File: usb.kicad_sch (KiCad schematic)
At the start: 37 parts, among them U1 MPFS250T-FCVG484, U12 SN74LVC1G04_SOT, U13 USB3340-EZK-TR, Y1 Resonator_24MHz_CTS_SA324

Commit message: [#54828] Add USB hub, change LBEE5PK2AE connection to USB
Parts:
- added U20: USB3803, antmicro-footprints:WLCSP-25_2.05x2.05mm_Layout5x5_P0.4x0.4mm_NSMD, symbol antmicroInterfaceControllers:USB3803
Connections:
- net USB_N: now also U20.E1 (USBUP_DM)
- net USB_P: now also U20.E2 (USBUP_DP)
- new net CONN_USB_N: U20.D1 (USBDN3_DM)
- new net CONN_USB_P: U20.C1 (USBDN3_DP)
- new net WL_BT_USB_DM: U20.D2 (USBDN2_DM)
- new net WL_BT_USB_DP: U20.C2 (USBDN2_DP)
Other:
- note added: "USB HUB"
- moved on the sheet: C118, C119, C120, C121, C122, C123, C124, D3, D4, D5, FB1, R58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

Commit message: [#54828] Add connections and external components to USB hub
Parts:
- added C258: C_1u_0402, antmicro-footprints:C_0402_1005Metric, symbol antmicroCapacitors0402:C_1u_0402
- added C259: C_4u7_0402, antmicro-footprints:C_0402_1005Metric, symbol antmicroCapacitors0402:C_4u7_0402
- added C260, C261, C262: C_100n_0402, antmicro-footprints:C_0402_1005Metric, symbol antmicroCapacitors0402:C_100n_0402
- added R100, R101, R102, R112, R113, R114, R115, R116, R117, R118, R119, R120, R98: R_10k_0402, antmicro-footprints:R_0402_1005Metric, symbol antmicroResistors0402:R_10k_0402
- added R99: R_12k_0402, antmicro-footprints:R_0402_1005Metric, symbol antmicroResistors0402:R_12k_0402
- added Y4: Oscillator_26MHz_ESC_2520MV, antmicro-footprints:Oscillator_SMD_ECS_2520MV_2.5x2mm, symbol antmicroOscillators:Oscillator_26MHz_ESC_2520MV
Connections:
- net +3V3: now also U20.B2 (VBAT), C260.2, C262.2, R100.2, R102.2, R113.2, R115.2, R98.2, Y4.1 (EN), Y4.4 (VDD)
- net CONN_USB_N: now also D4.2
- net CONN_USB_P: now also D5.2
- net GND: now also U20.C3 (GND), C258.1, C259.1, C260.1, C261.1, C262.1, R101.1, R112.1, R114.1, R116.1, R99.1, Y4.2 (GND)
- net USB_N: no longer D4.2
- net USB_OTG_ID: now also U20.A5 (BYPASS_N), R98.1
- net USB_P: no longer D5.2
- net SPK_L: now reaches R61.1, R62.2, TP2.1, U13.15 (SPK_L)
- net SPK_R: now reaches R59.1, R60.2, TP1.1, U13.16 (SPK_R)
- net VDD33_BYP: now reaches U20.A1 (USBDN1_DP)
- net VDD33_BYP: now also U20.A2 (VDD33_BYP), U20.B1 (USBDN1_DM), U20.B5 (HUB_CONNECT), C259.2
- net +1V8: now reaches U20.A3 (VDD_CORE_REG)
- net +1V8: now also C261.2
- net RBIAS: now reaches U20.A4 (RBIAS)
- net RBIAS: now also R99.2
- net REF_CLK: now reaches U20.B3 (REFCLK)
- net REF_CLK: now also Y4.3 (OUT)
- net I2C_ASEL1: now reaches U20.B4 (I2C_ASEL1)
- net I2C_ASEL1: now also R100.1, R101.2
- net I2C_ASEL0: now reaches U20.C4 (I2C_ASEL0)
- net I2C_ASEL0: now also R102.1, R112.2
- net USB_HUB_INT_N: now reaches U20.C5 (INT_N)
- net USB_HUB_INT_N: now also U1.D3 (MSSIO28B2), R119.1
- net VDD12_BYP: now reaches U20.D3 (VDD12_BYP)
- net VDD12_BYP: now also C258.2
- net REF_SEL1: now reaches U20.D4 (REF_SEL1)
- net REF_SEL1: now also R113.1, R114.2
- net USB_HUB_SDA: now reaches U20.D5 (SDA)
- net USB_HUB_SDA: now also U1.B1 (MSSIO27B2), R118.1
- net USB_HUB_RESET: now reaches U20.E3 (RESET_N)
- net USB_HUB_RESET: now also U1.C2 (MSSIO29B2), R120.1
- net REF_SEL0: now reaches U20.E4 (REF_SEL0)
- net REF_SEL0: now also R115.1, R116.2
- net USB_HUB_SCL: now reaches U20.E5 (SCL)
- net USB_HUB_SCL: now also U1.C1 (MSSIO26B2), R117.1
- new net VDDI: R117.2, R118.2, R119.2, R120.2
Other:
- note added: "HUB CLK"
- note added: "HUB FREQ CONFIG"
- note added: "HUB I2C ADDR CONFIG"
- note added: "I2C_ASEL[1:0]| I2C address '00' | 0x10 '01' | 0x11 '10' | 0x50 '11' | 0x51"
- note added: "REF_SEL[1:0] | Frequency (MHz) '00' | 38.4 '01' | 26.0 '10' | 19.2 '11' | 12.0"
- moved on the sheet: R64, TP1, TP2, TP3, TP4, U20

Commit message: [#54016] Change 100nF to 0201 package
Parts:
- C118, C119, C120, C121, C122, C123, C124: value C_100n_25V_0402 -> C_100n_0201_25V; footprint antmicro-footprints:C_0402_1005Metric -> antmicro-footprints:C_0201; symbol antmicroCapacitors0402:C_100n_25V_0402 -> antmicroCapacitorsmisc:C_100n_0201_25V; MPN CL05A104KA5NNNC -> C0603X5R1E104K030BB; Manufacturer Murata -> TDK
- C260, C261, C262: value C_100n_0402 -> C_100n_0201_25V; footprint antmicro-footprints:C_0402_1005Metric -> antmicro-footprints:C_0201; symbol antmicroCapacitors0402:C_100n_0402 -> antmicroCapacitorsmisc:C_100n_0201_25V; MPN GRM155R61H104KE14D -> C0603X5R1E104K030BB; Manufacturer Murata -> TDK; Voltage 50V -> 25V

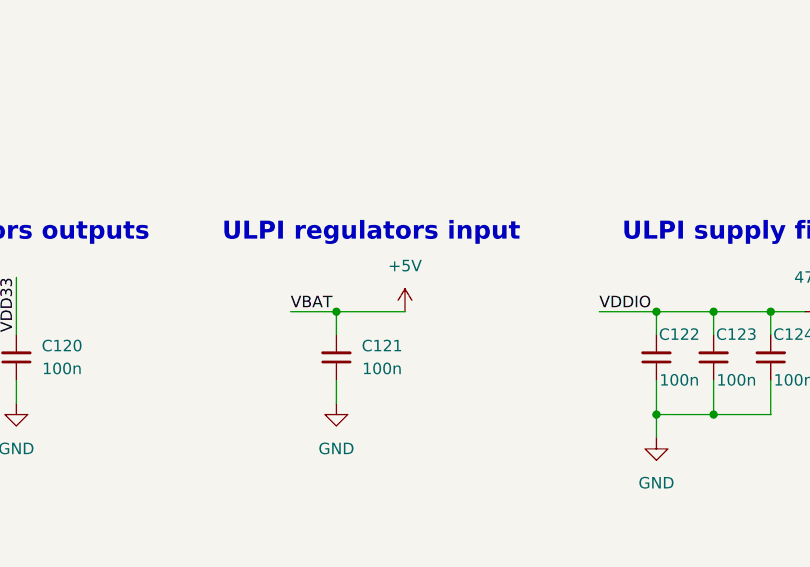
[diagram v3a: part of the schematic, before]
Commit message: [#54491] Change VBAT in USB Phy to 3V3
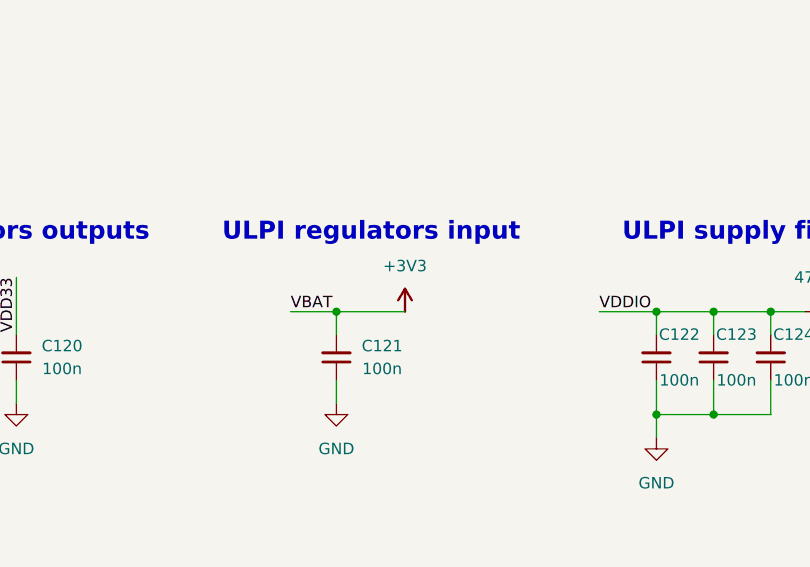
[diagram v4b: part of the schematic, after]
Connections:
- net +5V is gone; now on net +3V3: C121.2, U13.21 (VBAT)
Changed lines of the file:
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@@
     )
   )
+  (symbol (lib_id "antmicropower:+3V3") (at 85.09 57.15 0) (unit 1)
+    (in_bom yes) (on_board yes) (dnp no) (fields_autoplaced)
+    (property "Reference" "#PWR020" (at 100.33 59.69 0)
+      (effects (font (size 1.27 1.27) (thickness 0.15)) (justify left bottom) hide)
+    )
+    (property "Value" "+3V3" (at 85.09 52.07 0)
+      (effects (font (size 1.27 1.27) (thickness 0.15)))
+    )
+    (property "Footprint" "" (at 100.33 64.77 0)
+      (effects (font (size 1.27 1.27) (thickness 0.15)) (justify left bottom) hide)
+    )
+    (property "Datasheet" "" (at 100.33 67.31 0)
+      (effects (font (size 1.27 1.27) (thickness 0.15)) (justify left bottom) hide)
+    )
+    (property "Author" "Antmicro" (at 100.33 64.77 0)
+      (effects (font (size 1.27 1.27) (thickness 0.15)) (justify left bottom) hide)
+    )
+    (property "License" "Apache-2.0" (at 100.33 67.31 0)
+      (effects (font (size 1.27 1.27) (thickness 0.15)) (justify left bottom) hide)
+    )
+    (pin "1")
+    (instances
+      (project "polarfire-som"
+        (path "/db4a0d3e-2eb3-499e-977d-6eb378cfd3ed/d93d65d4-e21e-44e3-82fb-4ad52468a6b3"
+          (reference "#PWR020") (unit 1)
+        )
+      )
+    )
+  )
   (symbol (lib_id "antmicroResistors0402:R_10k_0402") (at 80.01 236.22 270) (mirror x) (unit 1)
     (in_bom yes) (on_board yes) (dnp no)
@@
         )
       )
-    )
-  )
-  (symbol (lib_id "antmicropower:+5V") (at 85.09 57.15 0) (unit 1)
-    (in_bom yes) (on_board yes) (dnp no) (fields_autoplaced)
-    (property "Reference" "#PWR0312" (at 100.33 59.69 0)
-      (effects (font (size 1.27 1.27) (thickness 0.15)) (justify left bottom) hide)
-    )
-    (property "Value" "+5V" (at 85.09 52.07 0)
-      (effects (font (size 1.27 1.27) (thickness 0.15)))
-    )
-    (property "Footprint" "" (at 100.33 64.77 0)
-      (effects (font (size 1.27 1.27) (thickness 0.15)) (justify left bottom) hide)
-    )
-    (property "Datasheet" "" (at 100.33 67.31 0)
-      (effects (font (size 1.27 1.27) (thickness 0.15)) (justify left bottom) hide)
-    )
-    (property "Author" "Antmicro" (at 100.33 64.77 0)
-      (effects (font (size 1.27 1.27) (thickness 0.15)) (justify left bottom) hide)
-    )
-    (property "License" "Apache-2.0" (at 100.33 67.31 0)
-      (effects (font (size 1.27 1.27) (thickness 0.15)) (justify left bottom) hide)
-    )
-    (pin "1")
-    (instances
-      (project "polarfire-som"
-        (path "/db4a0d3e-2eb3-499e-977d-6eb378cfd3ed/d93d65d4-e21e-44e3-82fb-4ad52468a6b3"
-          (reference "#PWR0312") (unit 1)
-        )
-      )

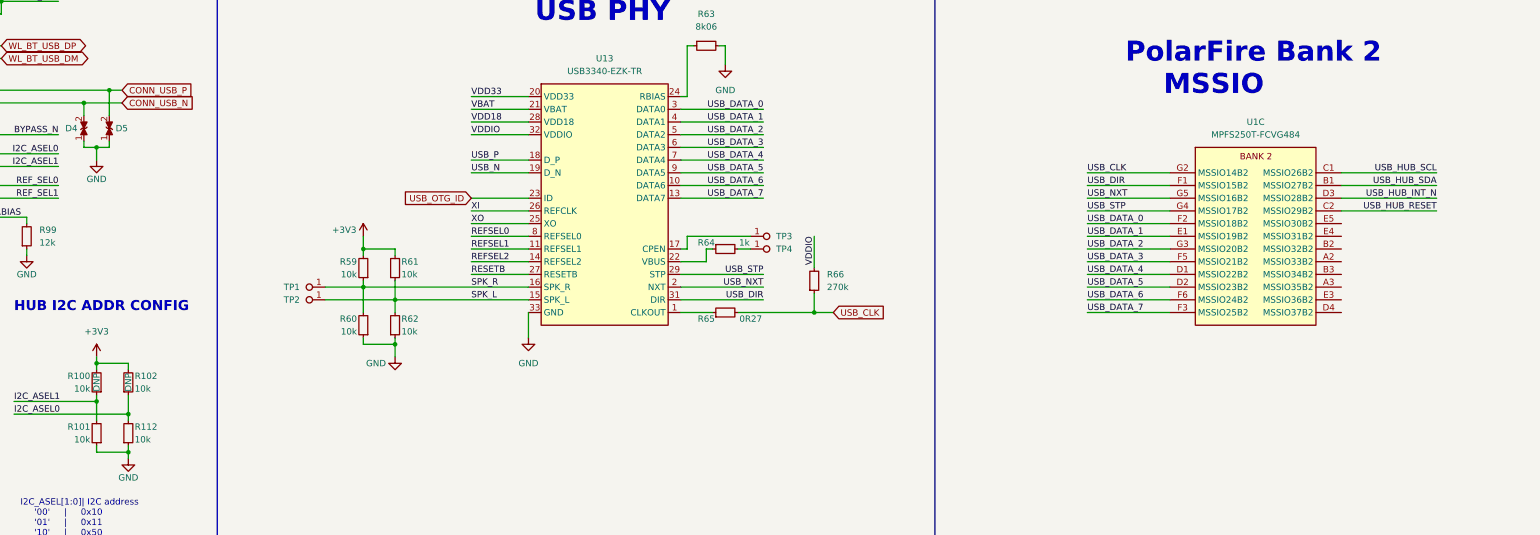
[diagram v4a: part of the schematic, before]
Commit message: [#54016] Add PAC1934 to MSSIO I2C_1, change USB hub default address
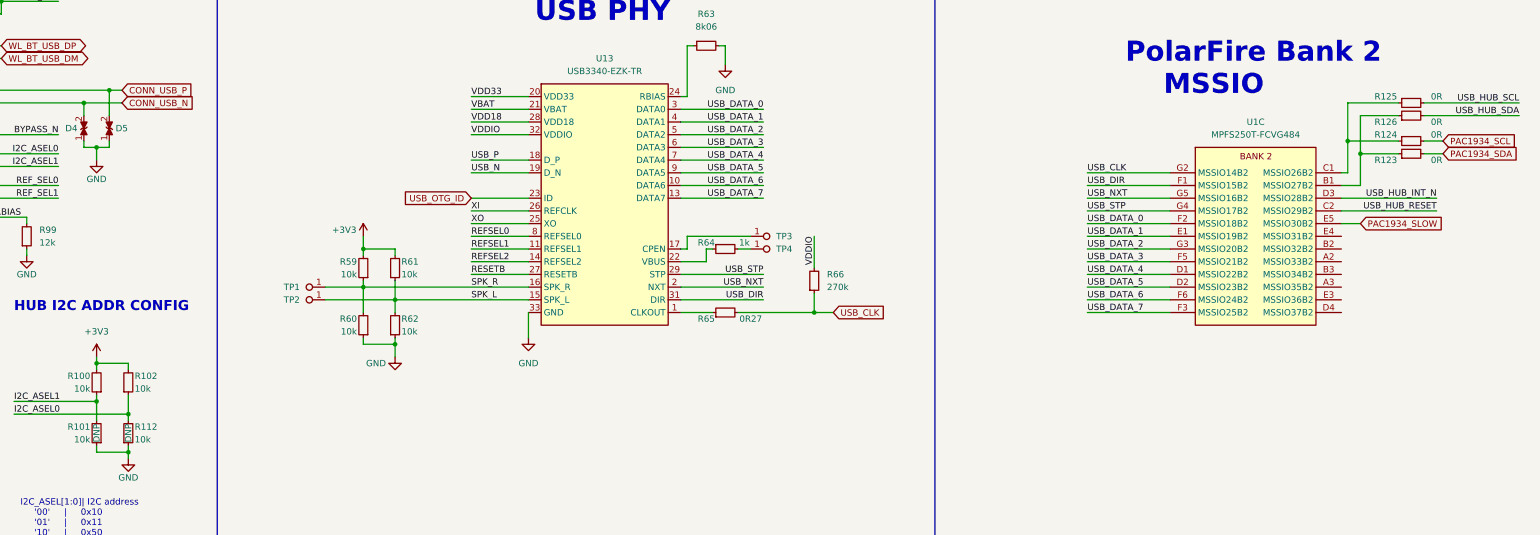
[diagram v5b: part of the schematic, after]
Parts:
- added R123, R124, R125, R126: R_0R_0402, antmicro-footprints:R_0402_1005Metric, symbol antmicroResistors0402:R_0R_0402
- R100, R102: DNP DNP -> (none); now in the parts list
- R101, R112: DNP (none) -> DNP; now left out of the parts list
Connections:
- net USB_HUB_SCL: now also R125.2; no longer U1.C1 (MSSIO26B2)
- net USB_HUB_SDA: now also R126.2; no longer U1.B1 (MSSIO27B2)
- net PAC1934_SLOW: now reaches U1.E5 (MSSIO30B2)
- new net: R123.1, R126.1, U1.B1 (MSSIO27B2)
- new net: R124.1, R125.1, U1.C1 (MSSIO26B2)
- new net PAC1934_SCL: R124.2
- new net PAC1934_SDA: R123.2

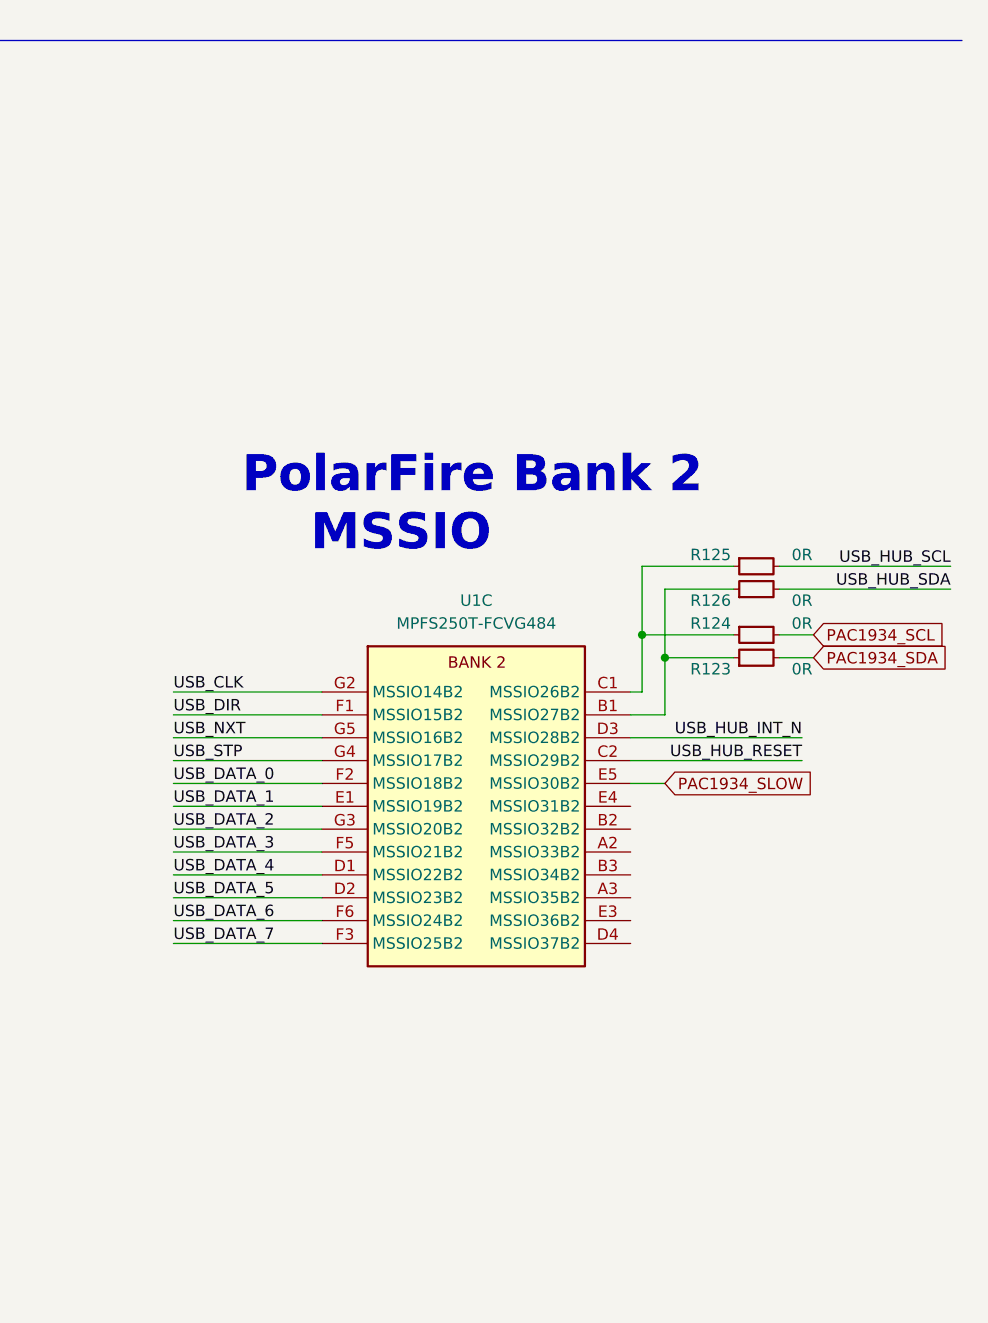
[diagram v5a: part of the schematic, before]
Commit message: [#54016] Add PMIC to MSSIO I2C_1
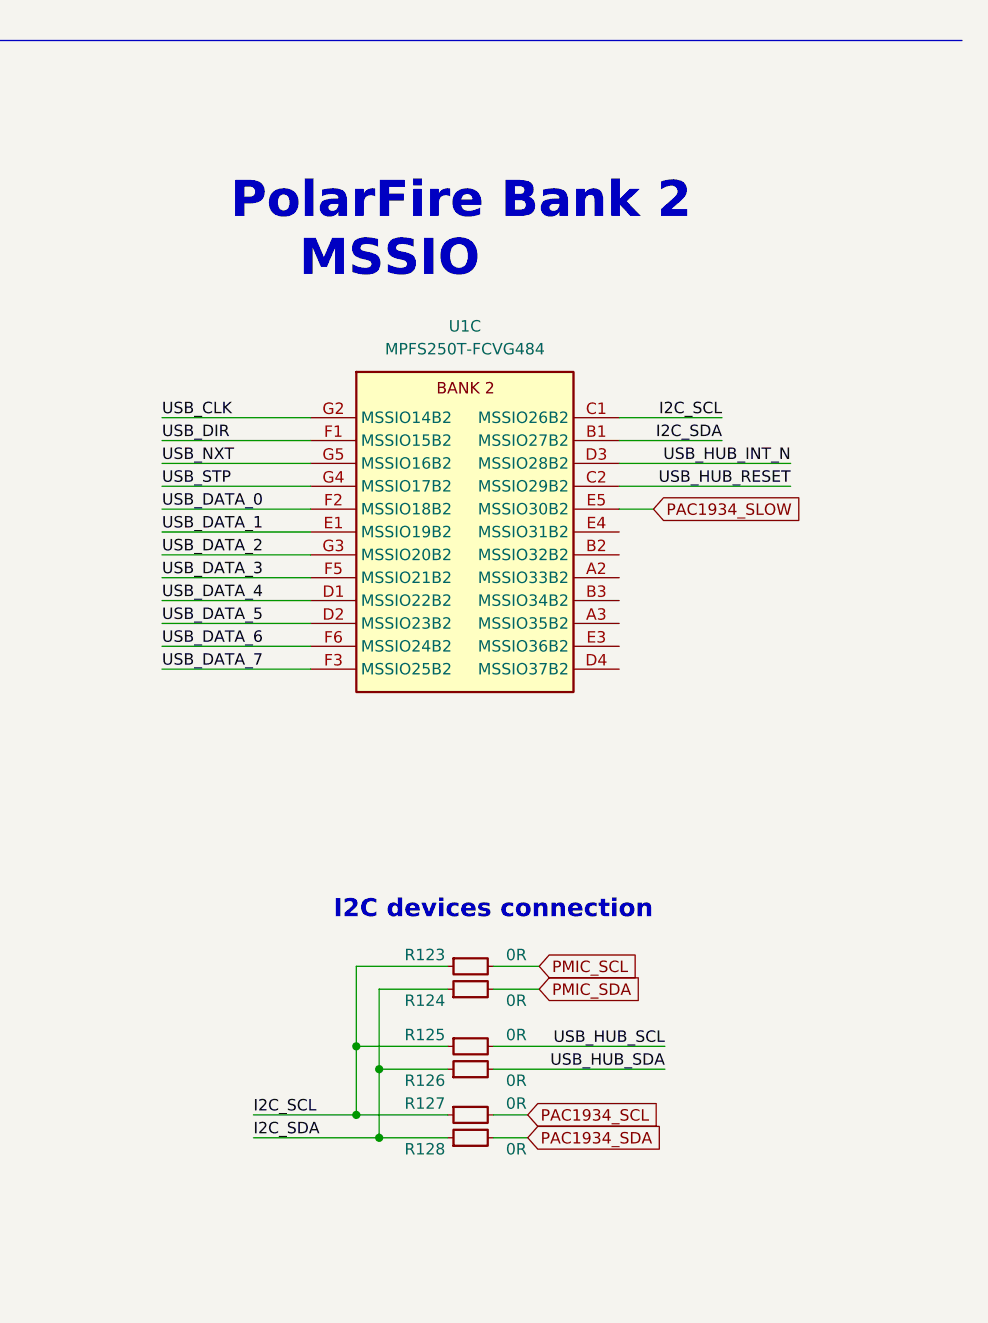
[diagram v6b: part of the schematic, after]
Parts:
- added R127, R128: R_0R_0402, antmicro-footprints:R_0402_1005Metric, symbol antmicroResistors0402:R_0R_0402
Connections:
- net PAC1934_SCL: now also R127.2; no longer R124.2
- net PAC1934_SDA: now also R128.2; no longer R123.2
- net I2C_SDA: now reaches R126.1, U1.B1 (MSSIO27B2)
- net I2C_SDA: now also R124.1, R128.1; no longer R123.1
- net I2C_SCL: now reaches R125.1, U1.C1 (MSSIO26B2)
- net I2C_SCL: now also R123.1, R127.1; no longer R124.1
- new net PMIC_SCL: R123.2
- new net PMIC_SDA: R124.2
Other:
- note added: "I2C devices connection"
- moved on the sheet: U1C

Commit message: [#54899] Add I2C connections
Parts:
- removed R117, R118: R_10k_0402, antmicro-footprints:R_0402_1005Metric, symbol antmicroResistors0402:R_10k_0402
- added R117, R118, R133, R47: R_0R_0402, antmicro-footprints:R_0402_1005Metric, symbol antmicroResistors0402:R_0R_0402
- added R45, R46: R_4k7_0402, antmicro-footprints:R_0402_1005Metric, symbol antmicroResistors0402:R_4k7_0402
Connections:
- net I2C_SCL: now also R117.1, R45.1, R47.1
- net I2C_SDA: now also R118.1, R133.1, R46.1
- net VDDI: now also R45.2, R46.2
- new net SN75_CTL_SCL: R117.2
- new net SN75_CTL_SDA: R118.2
- new net TPS_SCL: R47.2
- new net TPS_SDA: R133.2
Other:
- note added: "0x10"
- note added: "0x51"
- note added: "0x5E/0x38"
- note added: "0xBC"
- note added: "0xEC"
- note added: "Default addresses"
- note added: "HUB FREQ config"
- note added: "HUB I2C address config"
- note removed: "HUB FREQ CONFIG"
- note removed: "HUB I2C ADDR CONFIG"
- moved on the sheet: R123, R124, R125, R126, R127, R128

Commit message: [#54899] Re-annotate components
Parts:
- renumbered C261 to C176, C260 to C177, C262 to C178, C118 to C179, C120 to C180, C259 to C181, C258 to C182, C121 to C183, C122 to C184, C123 to C185, C124 to C186, C119 to C187, C125 to C188, C126 to C189, D4 to D2, D5 to D3, D3 to D4, R58 to R100, R64 to R101, R65 to R102, R66 to R103, R73 to R104, R45 to R105, R46 to R106, R123 to R107, R124 to R108, R125 to R109, R126 to R110, R127 to R111, R128 to R112, R47 to R113, R133 to R114, R117 to R115, R118 to R116, R119 to R77, R120 to R78, R113 to R79, R114 to R80, R115 to R81, R116 to R82, R99 to R83, R100 to R84, R101 to R85, R98 to R86, R102 to R87, R112 to R88, R67 to R89, R68 to R90, R59 to R91, R60 to R92, R69 to R93, R70 to R94, R61 to R95, R62 to R96, R71 to R97, R72 to R98, R63 to R99, TP3 to TP10, TP4 to TP11, TP1 to TP8, TP2 to TP9, U20 to U13, U13 to U14, U12 to U15, Y4 to Y1, Y1 to Y2
